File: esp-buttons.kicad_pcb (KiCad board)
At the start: 2 copper layers, 118.1 x 81.3 mm, 45 parts, among them CON1 POWER_5V, P1 CONN_BUTTON1, P2 CONN_BUTTON2, P3 CONN_BUTTON3, P4 CONN_BUTTON4, P5 CONN_BUTTON5, P6 UART_DEBUG, P7 UART, P8 POWER_5V, P9 USB, Q1 IRLML2502TRPBF, Q2 IRLML2502TRPBF, Q3 IRLML2502TRPBF, Q4 IRLML2502TRPBF, Q5 IRLML2502TRPBF, SW1 RESET_BUTTON, SW2 PROG_BUTTON, U1 ESP-07v2, U2 LD1117S33CTR, U3 FT230XS

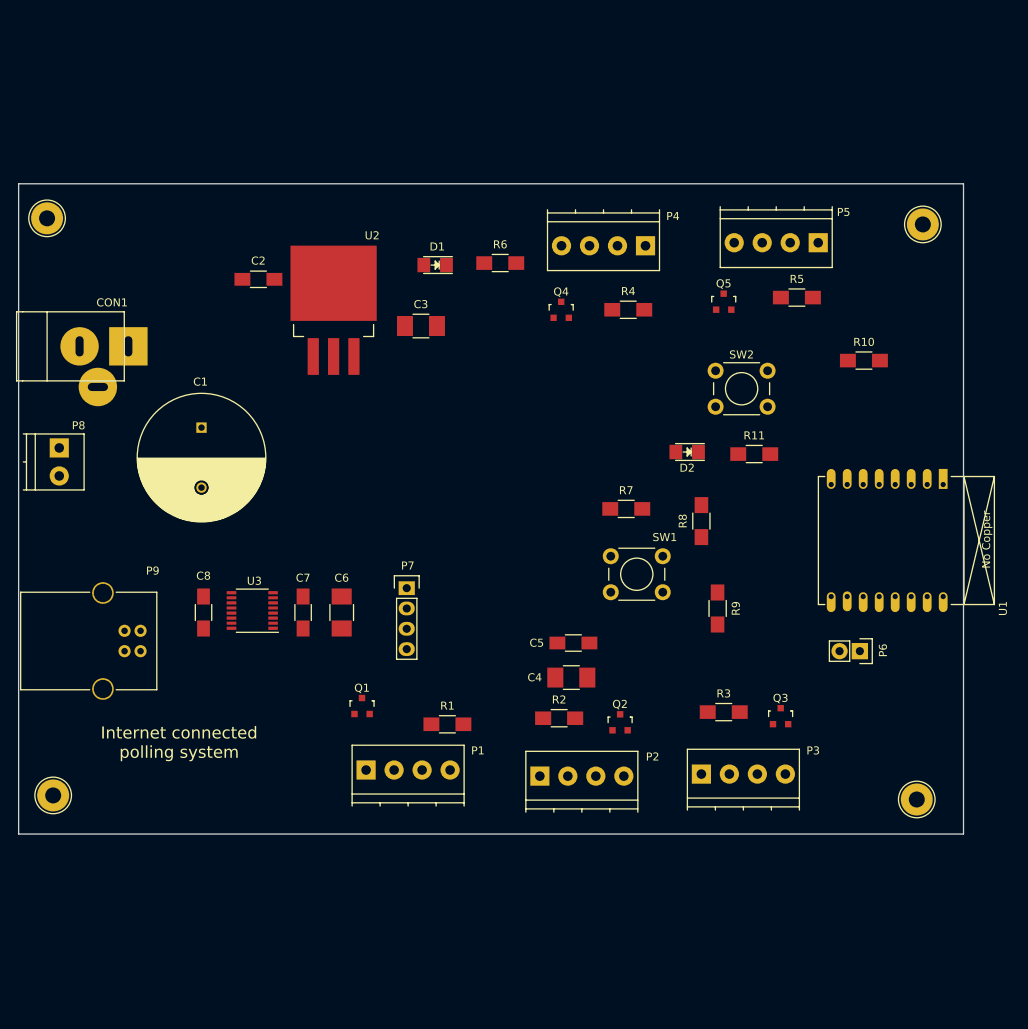
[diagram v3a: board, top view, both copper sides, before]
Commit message: Rotated the PCB on a more logical orientation
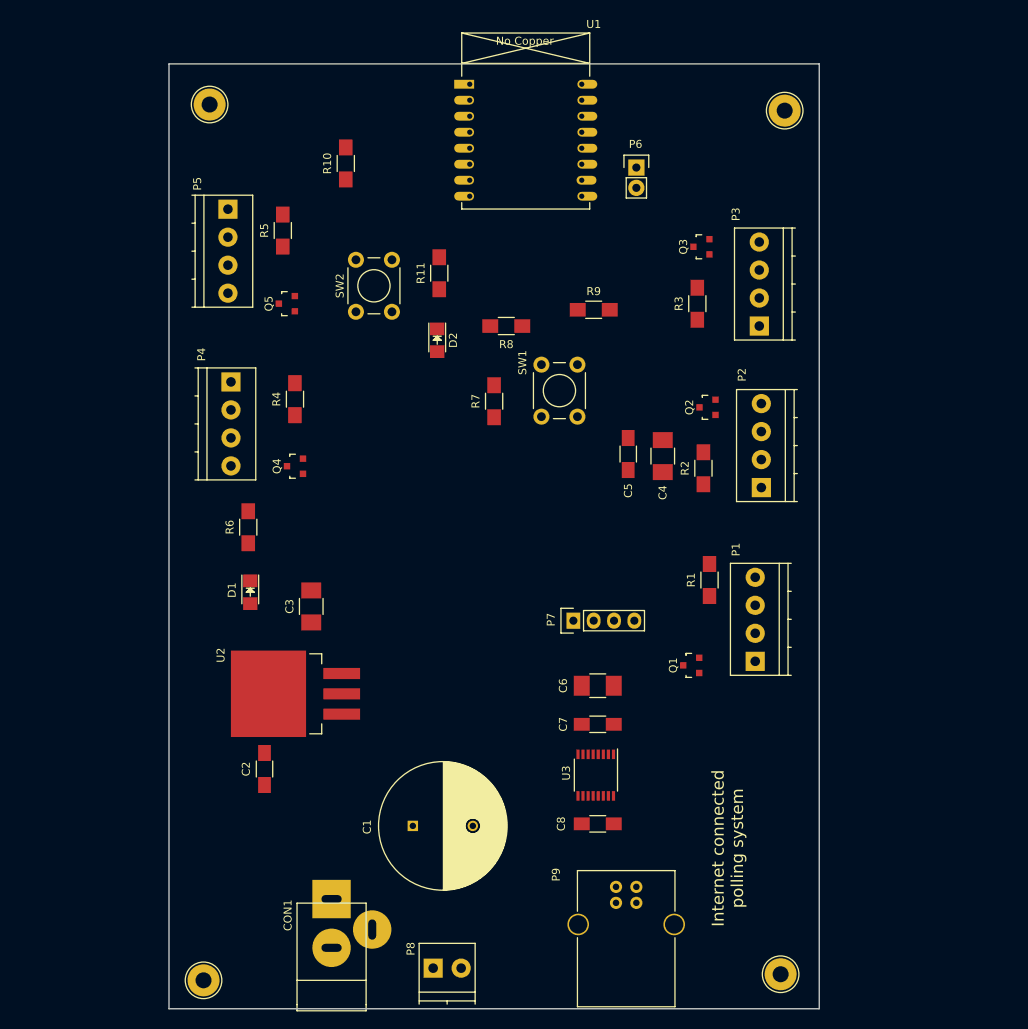
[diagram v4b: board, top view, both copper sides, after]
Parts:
- moved MT1 97.2 mm to (84.1, 170.7), turned to 90 degrees
- moved MT2 93.6 mm to (156.2, 169.9), turned to 90 degrees
- moved MT4 90.4 mm to (84.8, 61.2), turned to 90 degrees
- moved MT3 87.7 mm to (156.7, 62.0), turned to 90 degrees
- moved CON1 81.5 mm to (100.1, 166.6), turned to 90 degrees
- moved P8 80.1 mm to (112.8, 169.2), turned to 0 degrees
- moved U1 77.5 mm to (117.3, 58.7), turned to 0 degrees
- moved P5 73.9 mm to (87.1, 74.3), turned to 270 degrees
- moved R10 69.3 mm to (101.9, 68.6), turned to 90 degrees
- moved P9 68.6 mm to (138.2, 159.0), turned to 270 degrees
- moved P6 66.6 mm to (138.2, 69.1), turned to 0 degrees
- moved R5 64.8 mm to (94.0, 77.0), turned to 90 degrees
- moved C2 61.2 mm to (91.7, 144.3), turned to 90 degrees
- moved Q3 59.5 mm to (146.3, 79.0), turned to 90 degrees
- moved P3 56.5 mm to (153.5, 88.9), turned to 90 degrees
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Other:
- board size 118.1 x 81.3 mm -> 81.3 x 118.1 mm

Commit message: PCB settings. More component placement. Putting components' Value on the Silkscreen layer
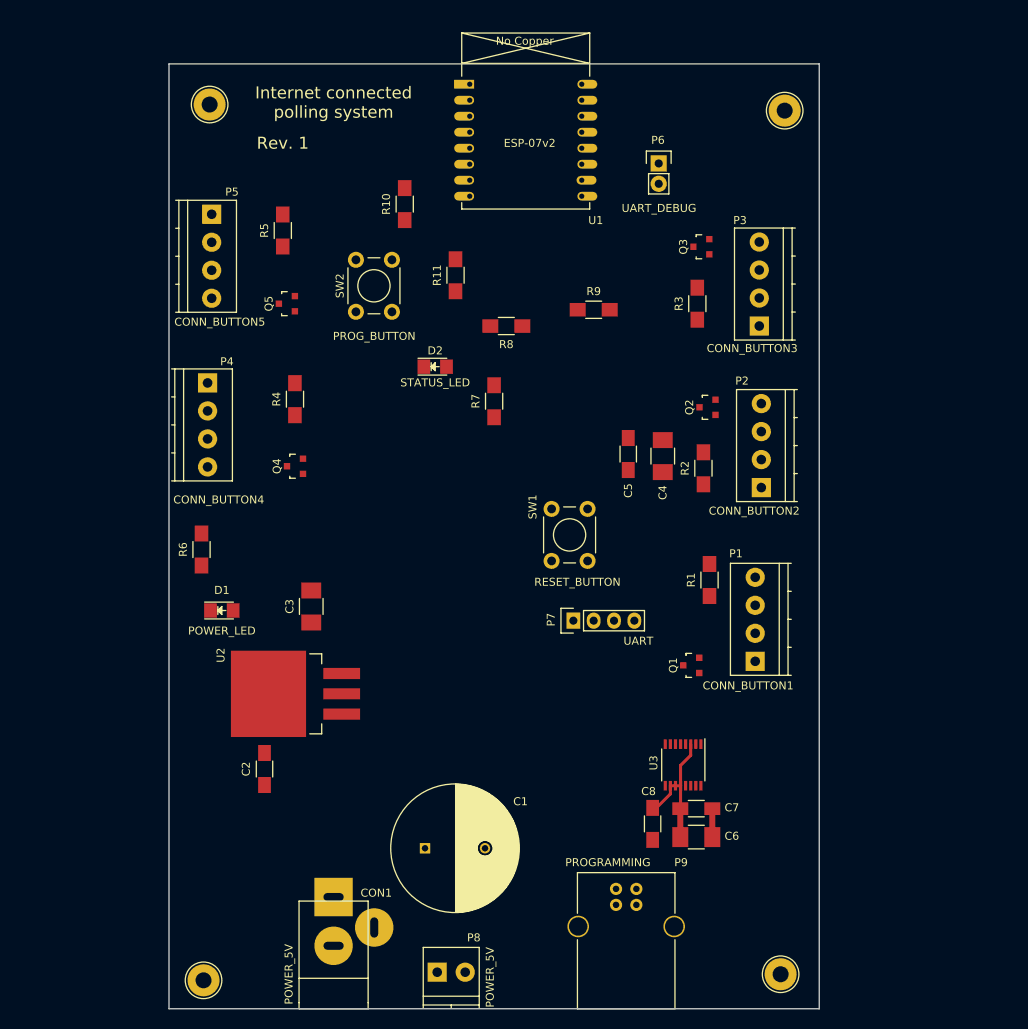
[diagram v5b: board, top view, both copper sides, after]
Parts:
- P9: value USB -> PROGRAMMING
- moved C6 22.6 mm to (145.7, 152.8), turned to 0 degrees
- moved SW1 18.1 mm to (132.1, 111.8)
- moved C7 16.2 mm to (145.7, 149.2), turned to 0 degrees
- moved U3 11.0 mm to (144.0, 143.8)
- moved R10 8.95 mm to (109.2, 73.7)
- moved C8 6.86 mm to (140.2, 151.1), turned to 270 degrees
- moved R6 6.48 mm to (83.8, 116.8)
- moved D1 4.23 mm to (86.4, 124.5), turned to 0 degrees
- moved D2 3.31 mm to (113.0, 94.0), turned to 0 degrees
- moved C1 3.18 mm to (111.8, 154.2)
- moved P4 2.92 mm to (84.6, 96.0)
- moved P6 2.84 mm to (141.0, 68.6)
- moved P5 2.13 mm to (85.1, 74.9)
- moved R11 2.05 mm to (115.6, 82.5)
- moved P8 0.72 mm to (113.3, 169.7)
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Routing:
- net +3V3: track 0.00 -> 17.5 mm
- net GND: track 0.00 -> 3.59 mm
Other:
- net class Default: trace_width 0.254 -> 0.762; via_dia 0.6 -> 1.016; via_drill 0.4 -> 0.508
- rule via_min_drill: 0.3 -> 0.254
- rule via_min_size: 0.4 -> 0.508
- board text added: "Rev. 1"

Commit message: More component placement and track layout done
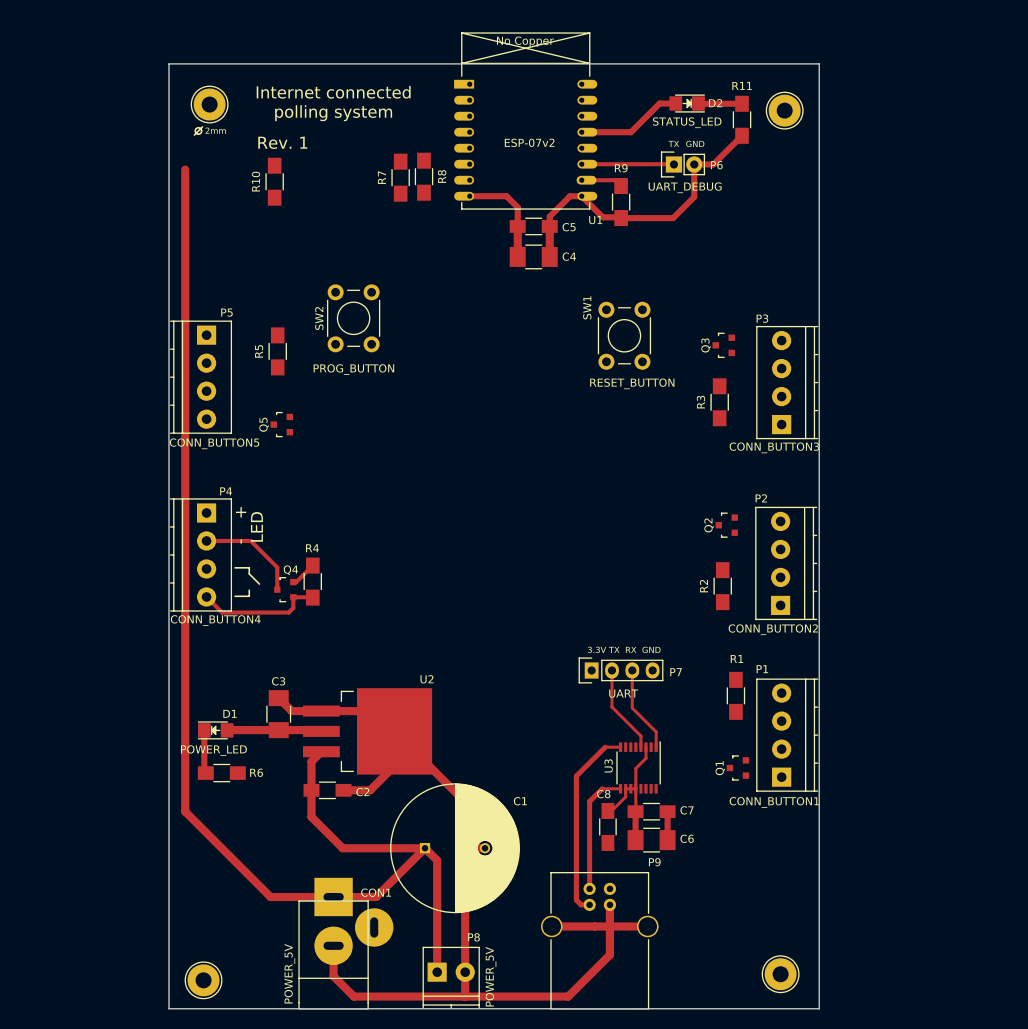
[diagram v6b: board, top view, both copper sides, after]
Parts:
- moved D2 45.5 mm to (144.5, 61.1), turned to 180 degrees
- moved R11 40.7 mm to (151.4, 63.1), turned to 270 degrees
- moved C5 30.8 mm to (125.3, 76.5), turned to 0 degrees
- moved R7 30.3 mm to (108.7, 70.4)
- moved C4 29.7 mm to (125.3, 80.3), turned to 0 degrees
- moved R6 28.1 mm to (86.4, 144.8), turned to 0 degrees
- moved SW1 25.8 mm to (138.9, 86.9)
- moved R4 22.9 mm to (97.7, 120.8)
- moved R8 21.3 mm to (111.6, 70.2), turned to 270 degrees
- moved R10 16.5 mm to (93.0, 70.9)
- moved P4 16.3 mm to (84.5, 112.3)
- moved Q4 15.5 mm to (94.3, 121.9)
- moved P5 15.1 mm to (84.5, 90.0)
- moved Q5 15.1 mm to (93.9, 101.2)
- moved R5 15.1 mm to (93.3, 92.1)
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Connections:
- U2 pad 4: (no net) -> GND
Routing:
- net GND: track 3.59 -> 174.4 mm
- net +5V: track 0.00 -> 157.8 mm
- net +3V3: track 17.5 -> 42.2 mm
- net /USB_D+: track 0.00 -> 24.4 mm
- net /BUTTON4: track 0.00 -> 15.7 mm
- net /USB_D-: track 0.00 -> 15.5 mm
- net /STATUS_LED: track 0.00 -> 13.2 mm
- net /LED4-: track 0.00 -> 13.0 mm
- net /UART_DEBUG_TX: track 0.00 -> 11.5 mm
- net /UART_TX: track 0.00 -> 11.1 mm
- net /UART_RX: track 0.00 -> 10.8 mm
- net Net-(D2-Pad1): track 0.00 -> 5.45 mm
- net Net-(D1-Pad1): track 0.00 -> 5.41 mm
- net Net-(R9-Pad1): track 0.00 -> 5.23 mm
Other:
- net class Default: trace_width 0.762 -> 0.508
- net class POWER added: clearance 0.254, trace_width 0.762, via_dia 1.016, via_drill 0.508
- board text added: "+"
- board text added: "-"
- board text added: "2mm"
- board text added: "3.3V TX RX GND"
- board text added: "GND"
- board text added: "LED"
- board text added: "TX"

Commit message: More component placement and track layout done. Exchanged the connections of two buttons on the ESP's pins
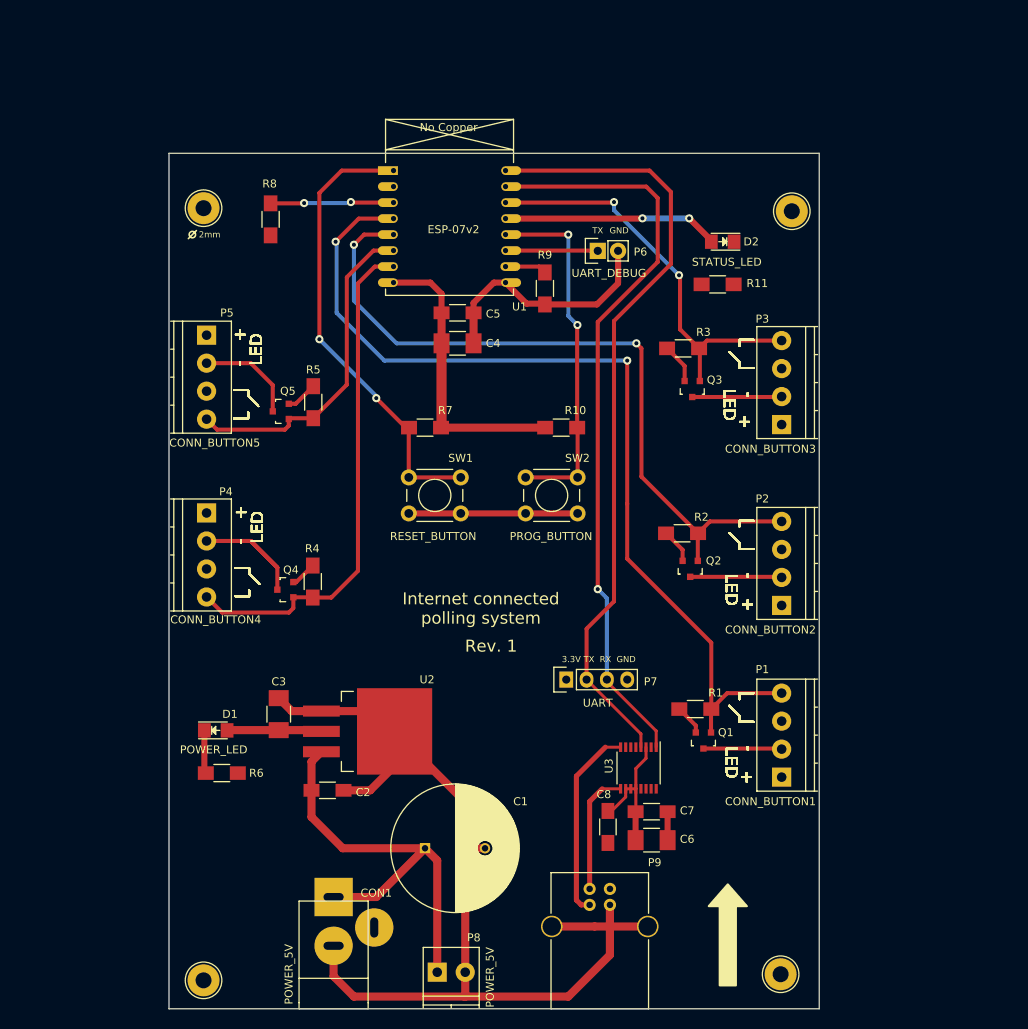
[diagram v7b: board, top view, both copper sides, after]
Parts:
- P9: value PROGRAMMING -> USB
- moved R10 47.2 mm to (128.8, 101.6), turned to 0 degrees
- moved SW1 35.9 mm to (109.7, 107.8), turned to 0 degrees
- moved R7 31.4 mm to (111.8, 101.6), turned to 180 degrees
- moved SW2 29.0 mm to (124.3, 107.8), turned to 0 degrees
- moved R11 20.8 mm to (148.3, 83.7), turned to 180 degrees
- moved R8 19.9 mm to (92.5, 75.6), turned to 90 degrees
- moved D2 17.8 mm to (149.0, 78.4)
- moved C4 14.4 mm to (115.8, 91.1)
- moved C5 14.4 mm to (115.8, 87.2)
- moved P6 14.4 mm to (133.3, 79.5)
- moved U1 14.4 mm to (107.8, 69.5)
- moved R9 14.4 mm to (126.7, 84.2)
- moved MT4 13.0 mm to (84.1, 74.2)
- moved MT3 12.6 mm to (157.6, 74.5)
- moved R2 8.33 mm to (143.9, 114.8), turned to 180 degrees
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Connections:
- U1 pad 14: /BUTTON5 -> /BUTTON3
- U1 pad 6: /BUTTON3 -> /BUTTON5
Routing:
- net /BUTTON1: track 0.00 -> 116.7 mm, vias 0 -> 2
- net +5V: track 157.8 -> 54.6 mm
- net /BUTTON2: track 0.00 -> 91.4 mm, vias 0 -> 2
- net /UART_TX: track 11.1 -> 98.4 mm
- net /UART_RX: track 10.8 -> 94.4 mm, vias 0 -> 1
- net /RESET: track 0.00 -> 57.4 mm, vias 0 -> 2
- net /BUTTON3: track 0.00 -> 51.1 mm, vias 0 -> 2
- net /BUTTON4: track 15.7 -> 64.0 mm
- net /PROG: track 0.00 -> 45.3 mm, vias 0 -> 2
- net /BUTTON5: track 0.00 -> 41.5 mm
- net GND: track 174.4 -> 205.1 mm
- net +3V3: track 42.2 -> 65.8 mm
- net Net-(R8-Pad2): track 0.00 -> 15.5 mm, vias 0 -> 2
- net /STATUS_LED: track 13.2 -> 27.0 mm, vias 0 -> 2
- net /LED5-: track 0.00 -> 12.7 mm
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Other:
- board size 81.3 x 118.1 mm -> 81.3 x 106.9 mm

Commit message: Track layout - part3
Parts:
- moved D1 9.16 mm to (88.6, 148.1)
- moved R6 9.16 mm to (89.4, 153.4)
- moved D2 2.17 mm to (151.0, 77.6)
- moved R11 2.17 mm to (150.4, 82.9)
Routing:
- net +3V3: track 65.8 -> 291.9 mm, vias 0 -> 3
- net +5V: track 54.6 -> 258.9 mm, vias 0 -> 1
- net GND: track 205.1 -> 251.2 mm, vias 0 -> 1
- net /BUTTON3: track 51.1 -> 58.5 mm
- net Net-(D2-Pad1): track 0.00 -> 5.36 mm
- net /STATUS_LED: track 27.0 -> 28.8 mm
- net /BUTTON1: track 116.7 -> 115.9 mm
- added copper zone on F.Cu, net GND
